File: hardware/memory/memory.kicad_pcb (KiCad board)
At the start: 2 copper layers, 77 x 77 mm, 76 parts, among them J1 Conn_Mem, J2 Conn_Power, J3 Conn_Mem_Ext, U1 74HC161, U10 74HC595, U11 74HC595, U12 74HC595, U13 74HC595, U14 74HC597, U15 74HC74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

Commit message: Added test points
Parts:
- added TP1: TestPoint, TestPoint:TestPoint_THTPad_D2.0mm_Drill1.0mm, F.Cu at (152.8, 93.6)
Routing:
- net GND: track 535.7 -> 537.4 mm
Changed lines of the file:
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@@
     (thickness 1.6)
     (drawings 18)
-    (tracks 1611)
+    (tracks 1613)
     (zones 0)
-    (modules 76)
+    (modules 77)
     (nets 126)
   )
@@
   )
   (setup
-    (last_trace_width 0.25)
+    (last_trace_width 0.35)
     (user_trace_width 0.35)
     (user_trace_width 0.5)
@@
       (xy 0.1016 -0.166391)) (layer B.SilkS) (width 0.01))
   )
+  (module TestPoint:TestPoint_THTPad_D2.0mm_Drill1.0mm (layer F.Cu)
+    (at 152.8 93.6)
+    (descr "THT pad as test Point, diameter 2.0mm, hole diameter 1.0mm")
+    (tags "test point THT pad")
+    (attr virtual)
+    (fp_text reference TP1 (at 0 -1.998) (layer F.SilkS) hide
+      (effects (font (size 1 1) (thickness 0.15)))
+    )
+    (fp_text value TestPoint (at 0 2.05) (layer F.Fab)
+      (effects (font (size 1 1) (thickness 0.15)))
+    )
+    (fp_text user %R (at 0 -2) (layer F.Fab)
+      (effects (font (size 1 1) (thickness 0.15)))
+    )
+    (fp_circle (center 0 0) (end 1.5 0) (layer F.CrtYd) (width 0.05))
+    (fp_circle (center 0 0) (end 0 1.2) (layer F.SilkS) (width 0.12))
+    (pad 1 thru_hole circle (at 0 0) (size 2 2) (drill 1) (layers *.Cu *.Mask)
+      (net 11 GND))
+  )
   (gr_text JLCJLCJLCJLC (at 145.5 123.25) (layer F.SilkS)
     (effects (font (size 1 1) (thickness 0.15)))
@@
   (segment (start 152.0325 101.555) (end 151.0325 101.555) (width 0.35) (layer B.Cu) (net 11))
   (segment (start 152.7075 101.555) (end 152.0325 101.555) (width 0.35) (layer B.Cu) (net 11))
-  (segment (start 151.0325 101.555) (end 151.0325 88.6975) (width 0.35) (layer B.Cu) (net 11))
   (segment (start 152.0325 78.695) (end 152.7075 78.695) (width 0.35) (layer B.Cu) (net 11))
   (segment (start 151.51 78.695) (end 152.0325 78.695) (width 0.35) (layer B.Cu) (net 11))
@@
   (segment (start 163.4 122.4) (end 163.4075 122.4075) (width 0.35) (layer B.Cu) (net 11))
   (segment (start 177.935 72.8) (end 177.935 73.86) (width 0.35) (layer B.Cu) (net 11))
+  (segment (start 151.0325 101.555) (end 151.0325 93.6) (width 0.35) (layer B.Cu) (net 11))
+  (segment (start 151.0325 93.6) (end 151.0325 88.6975) (width 0.35) (layer B.Cu) (net 11))
+  (segment (start 151.0325 93.6) (end 152.8 93.6) (width 0.35) (layer B.Cu) (net 11))
   (segment (start 169.29 82.493591) (end 169.925 83.128591) (width 0.25) (layer F.Cu) (net 12))
   (segment (start 169.29 80.4425) (end 169.29 82.493591) (width 0.25) (layer F.Cu) (net 12))

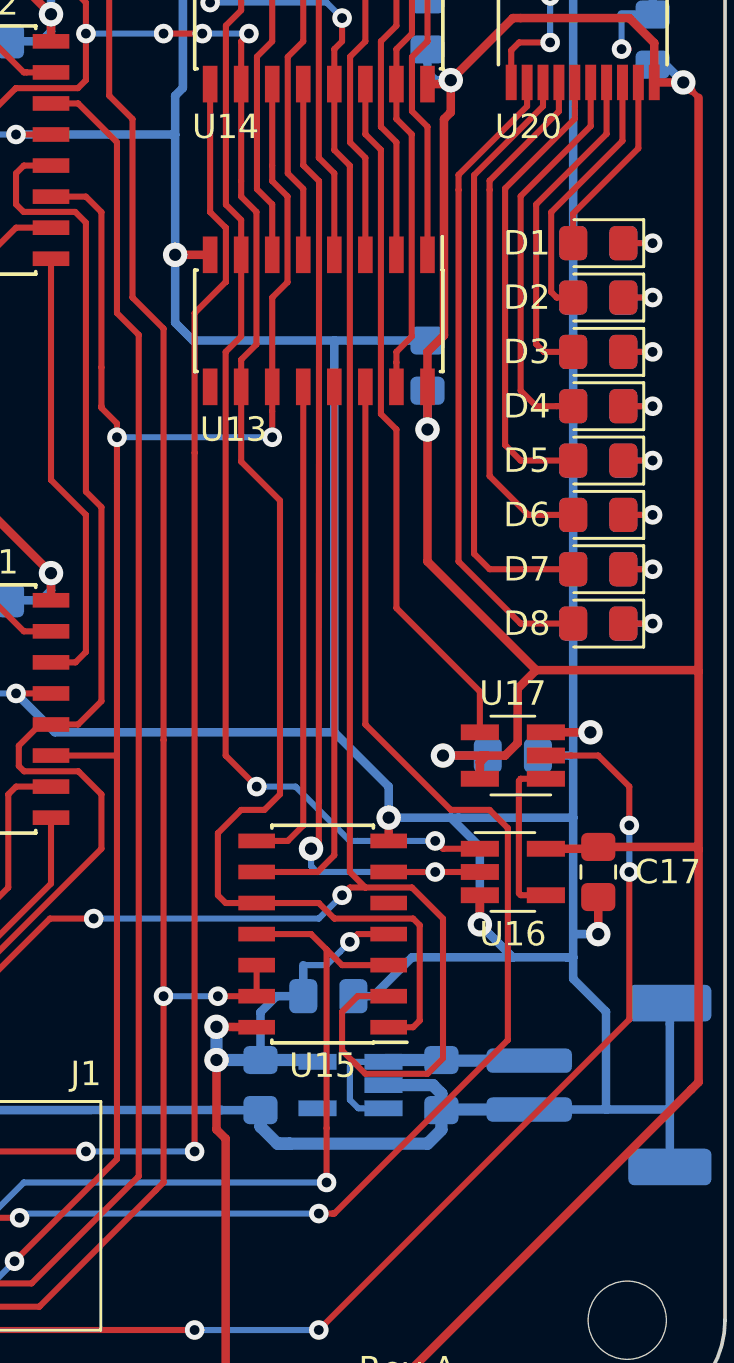
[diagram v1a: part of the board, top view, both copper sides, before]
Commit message: Sign bit is D7. Change 74LVC1G38 to 74LVC1G00
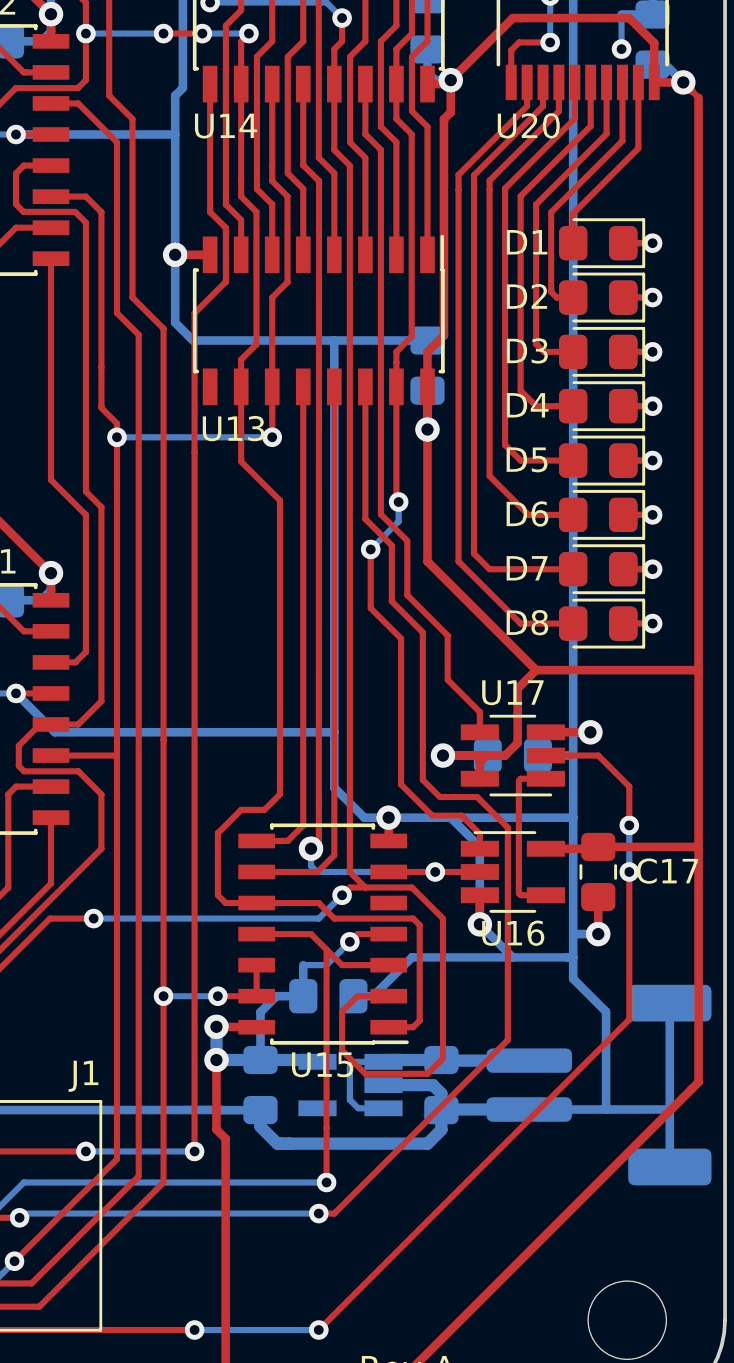
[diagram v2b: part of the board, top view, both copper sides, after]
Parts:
- U21: value 74LVC1G38 -> 74LVC1G00
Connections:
- U16 pad 1: /D0 -> /D7
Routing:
- net /D0: track 99.4 -> 66.6 mm, vias 3 -> 1
- net /D7: track 47.9 -> 69.8 mm, vias 0 -> 2
- net GND: track 537.4 -> 538.0 mm

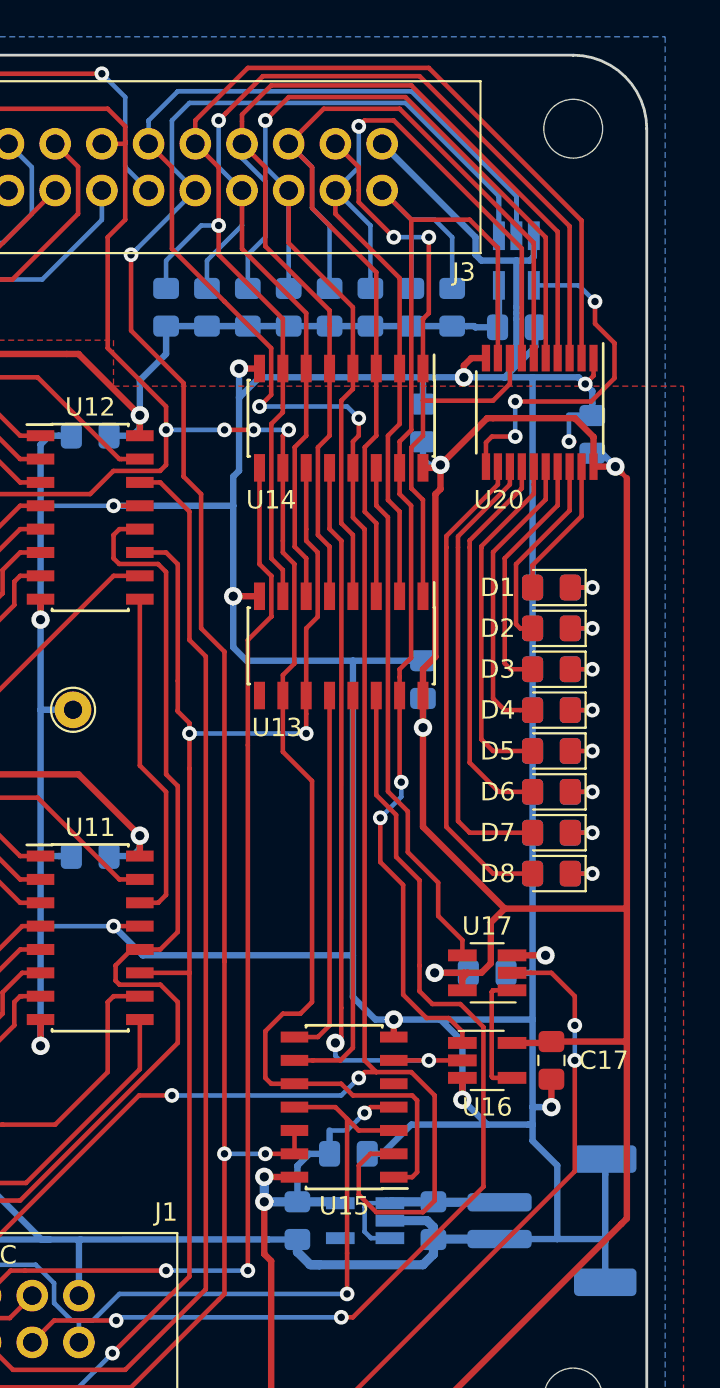
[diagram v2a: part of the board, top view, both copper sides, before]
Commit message: Fixed LED latch
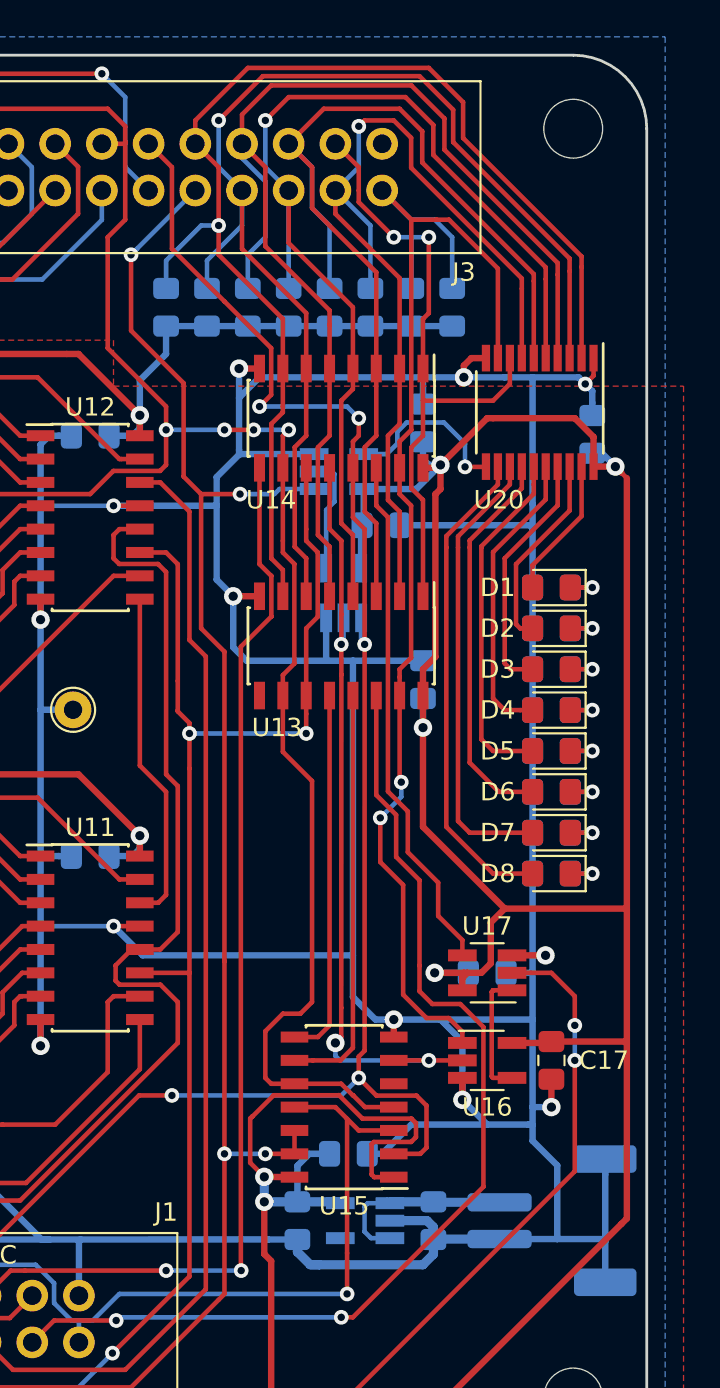
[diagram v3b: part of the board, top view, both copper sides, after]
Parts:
- added U22: 74LVC1G32, Package_TO_SOT_SMD:SOT-23-5_HandSoldering, B.Cu at (167.5, 87.2)
- moved U21 15.0 mm to (167.3, 80.6), turned to 0 degrees
- moved C21 13.0 mm to (169.5, 83.6)
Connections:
- U15 pad 1: /~RESET -> VCC
- U15 pad 4: VCC -> /~RESET
- U21 pad 2: /~MEM_OE -> Net-(U21-Pad2)
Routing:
- net /~MEM_OE: track 134.8 -> 97.2 mm, vias 4 -> 5
- net /~MEM_WE: track 116.4 -> 94.1 mm, vias 3 -> 4
- net VCC: track 491.8 -> 509.8 mm, vias 20 -> 19
- net GND: track 538.0 -> 527.1 mm, vias 26 -> 25
- net /LED_LATCH: track 19.2 -> 9.48 mm, vias 3 -> 1
- net Net-(U21-Pad2): track 0.00 -> 6.47 mm
- net /~RESET: track 291.4 -> 285.0 mm
- net /DOUT_LATCH: track 41.3 -> 42.8 mm, vias 2 -> 3
- net /D7: track 69.8 -> 69.2 mm
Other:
- board text added: "Rev B 2021-09-03"
- board text removed: "2020-06-11"

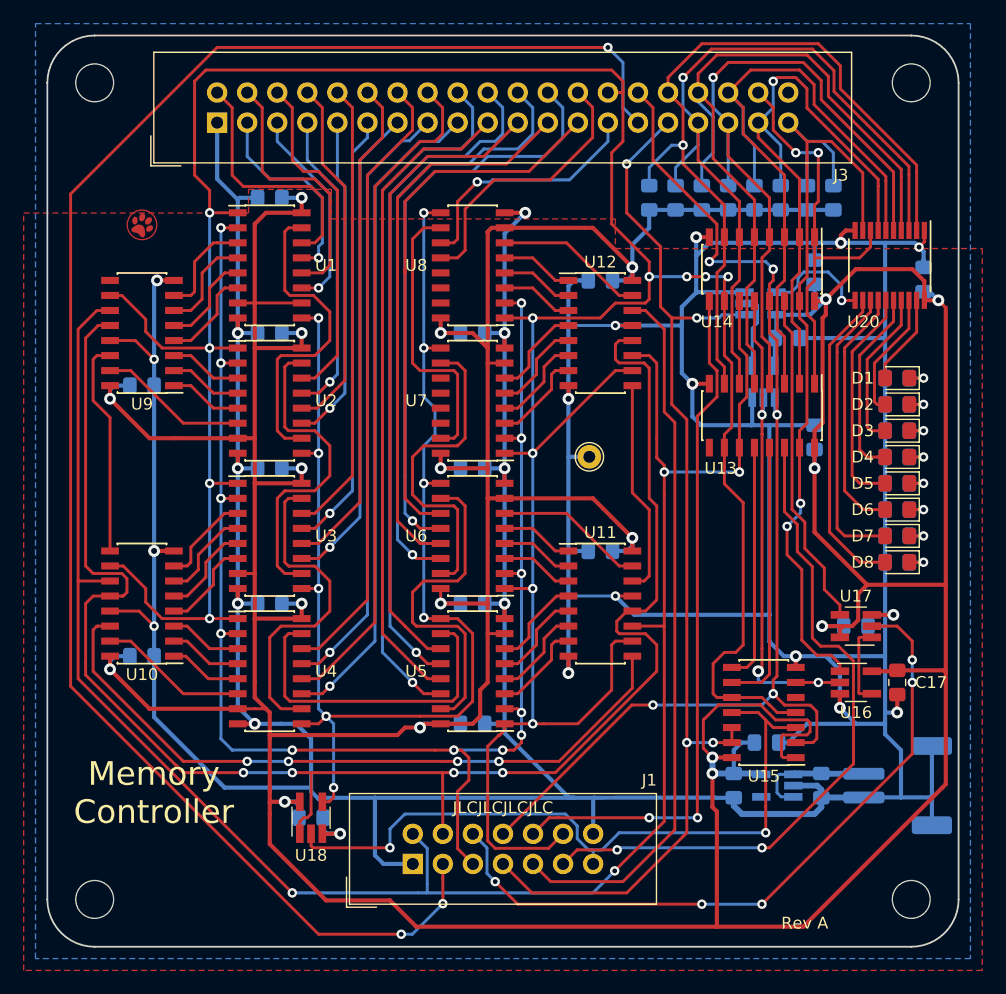
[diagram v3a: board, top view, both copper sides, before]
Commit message: Update all to Kicad 6
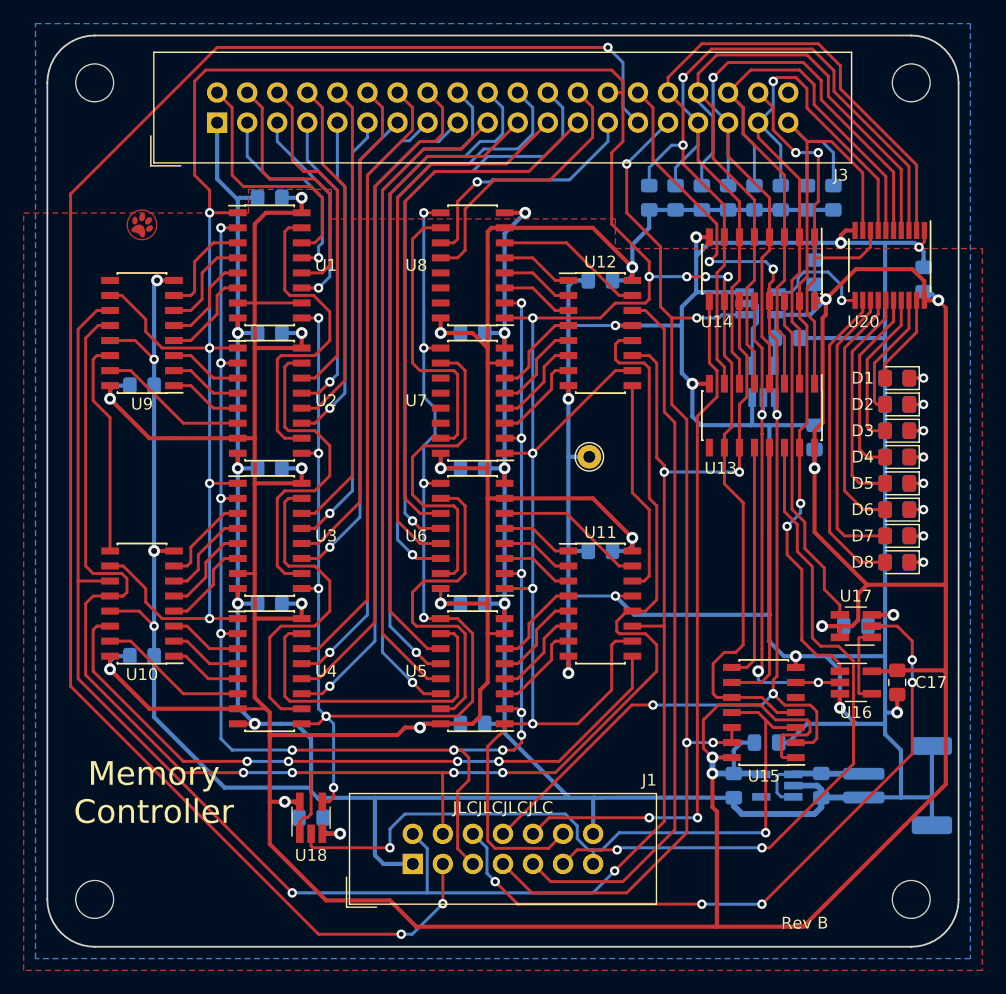
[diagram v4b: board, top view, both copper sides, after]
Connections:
- net /~ADDR_PE renamed /~{ADDR_PE}
- net /~DIN_OE renamed /~{DIN_OE}
- net /~MEM_OE renamed /~{MEM_OE}
- net /~MEM_WE renamed /~{MEM_WE}
- net /~RESET renamed /~{RESET}
- net /~SIGN? renamed /~{SIGN?}
- net /~S_EXT renamed /~{S_EXT}
- net /~WAIT renamed /~{WAIT}
- U13 pad 9: Net-(U13-Pad9) -> unconnected-(U13-Pad9)
- U15 pad 5: Net-(U15-Pad5) -> unconnected-(U15-Pad5)
- U19 pad 4: Net-(U19-Pad4) -> unconnected-(U19-Pad4)
- U8 pad 15: Net-(U8-Pad15) -> unconnected-(U8-Pad15)
- U9 pad 9: Net-(U9-Pad9) -> unconnected-(U9-Pad9)
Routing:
- net VCC: track 509.8 -> 507.9 mm
- net /ADDR_LATCH: track 140.2 -> 139.3 mm
- net GND: track 527.1 -> 526.2 mm
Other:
- net class Default removed
- board text added: "2021-09-03"
- board text added: "Rev B"
- board text removed: "Rev A"
- board text removed: "Rev B 2021-09-03"
